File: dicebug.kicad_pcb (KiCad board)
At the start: 2 copper layers, 47.3 x 40.9 mm, 56 parts, among them J3 PMOD, Q1 SSM6N35AFE, U1 74LV163ADR, U2 MTCH1010, U3 74HCS7266DR, U4 MIC5205YM5, U5 iqs211a

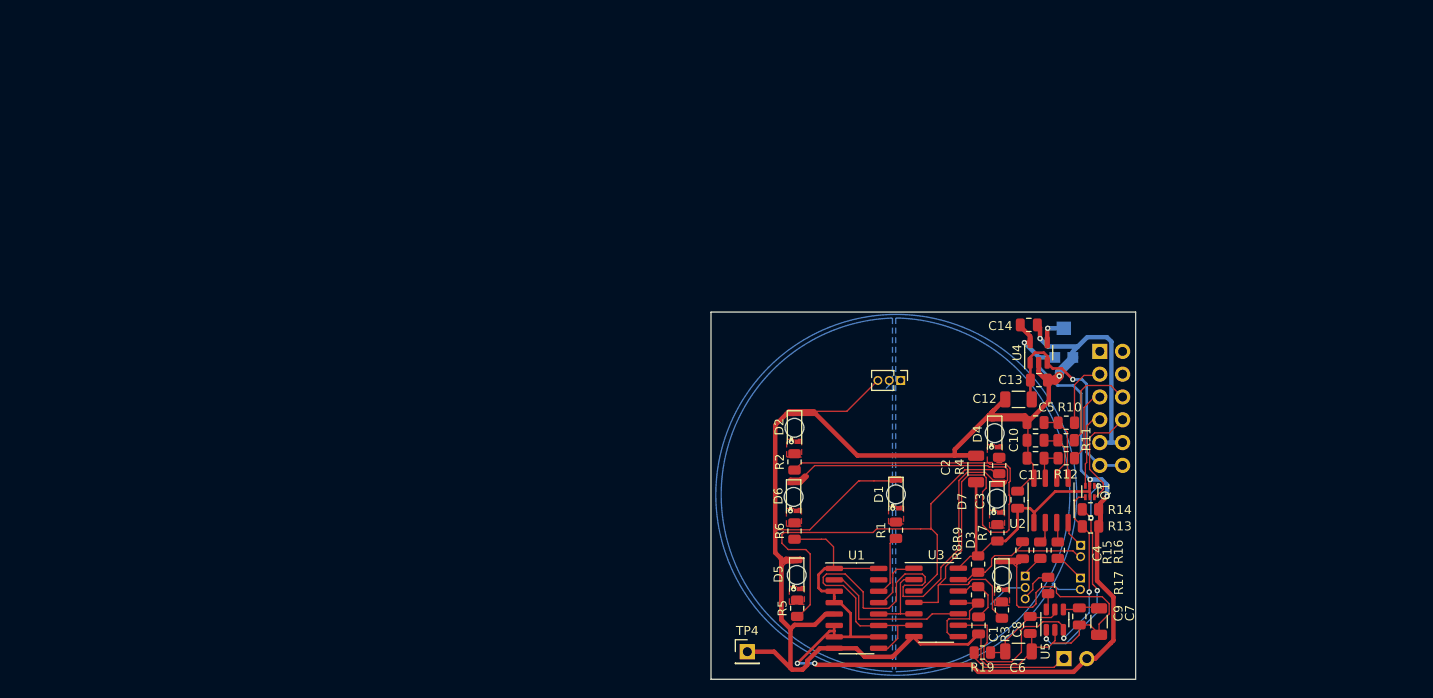
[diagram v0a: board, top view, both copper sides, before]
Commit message: almost finalized with individual LED resistors, though
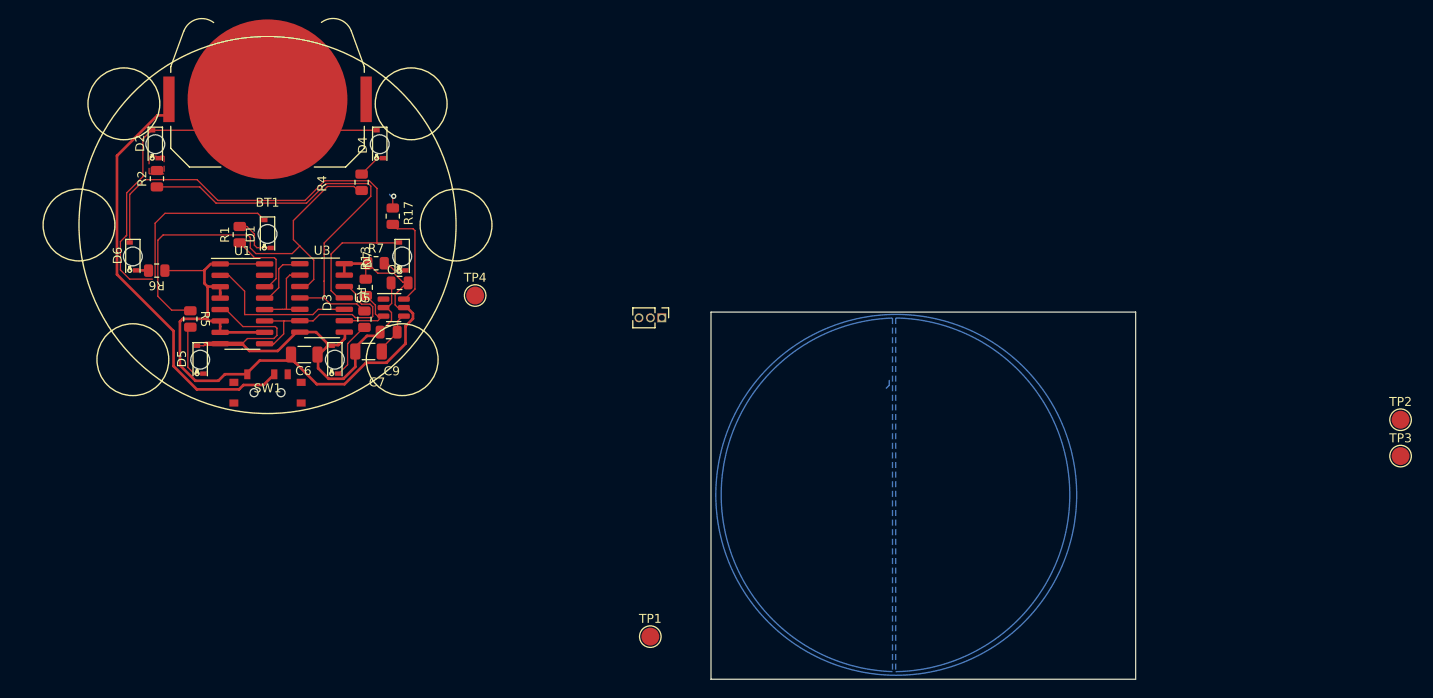
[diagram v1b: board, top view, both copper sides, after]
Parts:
- removed C1, C10, C11, C13, C5: 10n, Capacitor_SMD:C_0805_2012Metric
- removed C12, C2: 1u, Capacitor_SMD:C_1206_3216Metric
- removed C14: 1u, Capacitor_SMD:C_0805_2012Metric
- removed C3, C4: 100n, Capacitor_SMD:C_0805_2012Metric
- removed J3: PMOD, proj_footprints:PMOD_PinHeader_2x06_P2.54mm_Horizontal
- removed JP1: PWR_IQS, Connector_PinHeader_2.54mm:PinHeader_1x02_P2.54mm_Vertical
- removed JP2: MTCH, Connector_PinHeader_1.27mm:PinHeader_1x02_P1.27mm_Vertical
- removed JP3: i SENS m, Connector_PinHeader_1.27mm:PinHeader_1x03_P1.27mm_Vertical
- removed JP4: SHLD, Connector_PinHeader_1.27mm:PinHeader_1x02_P1.27mm_Vertical
- removed Q1: SSM6N35AFE, proj_footprints:SOT-563-adjusted
- removed R10, R11, R12, R14, R15, R8, R9: 100k, Resistor_SMD:R_0805_2012Metric
- removed R16: 1k, Resistor_SMD:R_0805_2012Metric
- removed R19: 40, Resistor_SMD:R_0805_2012Metric
- removed RV1: 100k, Potentiometer_SMD:Potentiometer_Bourns_TC33X_Vertical
- removed U2: MTCH1010, Package_SO:SOIC-8_3.9x4.9mm_P1.27mm
- removed U4: MIC5205YM5, Package_TO_SOT_SMD:SOT-23-5
- added BT1: CR2032, Battery:BatteryHolder_Keystone_3034_1x20mm, F.Cu at (100.0, 86.0)
- added SW1: SW_SPDT, proj_footprints:450404015514, F.Cu at (100.0, 118.7)
- added TP3: SCL, TestPoint:TestPoint_Pad_D2.0mm, F.Cu at (226.2, 125.7)
- added TP4: SDA, TestPoint:TestPoint_Pad_D2.0mm, F.Cu at (123.1, 107.9)
- TP1: renamed from TP4; value TestPoint -> GND; footprint Connector_PinHeader_2.54mm:PinHeader_1x01_P2.54mm_Vertical -> TestPoint:TestPoint_Pad_D2.0mm
- TP2: value Shield -> VCC; footprint sensors:tp_end -> TestPoint:TestPoint_Pad_D2.0mm; moved to F.Cu
- moved C7 86.8 mm to (111.3, 114.1), turned to 180 degrees
- moved C6 86.2 mm to (104.1, 114.4)
- moved R13 85.0 mm to (110.9, 106.9), turned to -90 degrees
- moved R17 83.8 mm to (114.0, 99.0)
- moved C9 83.2 mm to (113.5, 111.9), turned to 180 degrees
- moved U5 81.4 mm to (114.1, 109.2), turned to 0 degrees
- moved TP5 81.1 mm to (113.6, 96.6)
- moved R1 80.2 mm to (96.9, 101.1)
- moved C8 79.9 mm to (114.7, 106.5), turned to 180 degrees
- moved D6 78.3 mm to (85.0, 103.5)
- moved D3 78.1 mm to (107.5, 115.0)
- moved R3 78.0 mm to (110.8, 110.5), turned to -90 degrees
- moved D2 77.9 mm to (87.5, 91.0)
- moved R4 77.7 mm to (110.5, 95.2)
- moved R2 77.7 mm to (87.7, 94.8)
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- renumbered TP1 to TP5, TP3 to TP6
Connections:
- C6 pad 1: Net-(U5-VDD) -> +3V0
- C8 pad 1: Net-(U5-VDD) -> +3V0
- JP5 pad 1: Net-(JP3-C) -> /SENS_IQS
- TP2 pad 1: Net-(JP4-B) -> +3V0
- TP5 pad 1: Net-(JP3-C) -> /SENS_IQS
- U1 pad 11: Net-(D6-K) -> Net-(U1-Q3)
- U1 pad 9: Net-(D6-K) -> Net-(U1-Q3)
- U3 pad 11: Net-(R8-Pad2) -> Net-(D6-K)
- U3 pad 12: Net-(C1-Pad1) -> Net-(U1-Q3)
- U3 pad 13: Net-(JP2-B) -> +3V0
- U3 pad 6: Net-(D6-K) -> Net-(U1-Q3)
- U3 pad 8: Net-(R8-Pad2) -> GND
- U5 pad 5: Net-(U5-VDD) -> +3V0
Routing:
- net GND: track 299.4 -> 104.7 mm, vias 2 -> 0
- net +3V0: track 161.9 -> 94.3 mm, vias 5 -> 0
- net Net-(BT1-+): track 0.00 -> 46.8 mm
- net Net-(D6-K): track 95.9 -> 55.8 mm
- net Net-(U5-IO2/SDA): track 39.4 -> 8.01 mm, vias 2 -> 0
- net +3V3: track 25.5 -> 0.00 mm, vias 1 -> 0
- net Net-(U5-IO1/SCL): track 24.9 -> 0.00 mm, vias 4 -> 0
- net Net-(U1-Q3): track 0.00 -> 23.5 mm
- net Net-(R2-Pad1): track 71.3 -> 47.9 mm
- net Net-(JP2-B): track 16.9 -> 0.00 mm
- net Net-(J3-Pin_10): track 12.1 -> 0.00 mm
- net Net-(JP1-A): track 11.4 -> 0.00 mm
- net /CFG1: track 11.2 -> 0.00 mm
- net Net-(U5-VDD): track 10.2 -> 0.00 mm
- net Net-(R8-Pad2): track 9.69 -> 0.00 mm
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- added copper zone on B.Cu, net (none)
- added copper zone on B.Cu, net /SENS_IQS
- removed copper zone on F.Cu, net Net-(D1-A)
- removed copper zone on F.Cu, net Net-(D3-A)
- removed copper zone on F.Cu, net Net-(D4-A)
- removed copper zone on F.Cu, net Net-(D5-A)
- removed copper zone on F.Cu, net Net-(D6-A)
- removed copper zone on F.Cu, net Net-(D7-A)
- removed copper zone on B.Cu, net Net-(JP3-C)
- removed copper zone on B.Cu, net Net-(JP4-B)
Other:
- board text added: "dicebug-1.0"
- board text removed: "dicebug-dev-1.0"

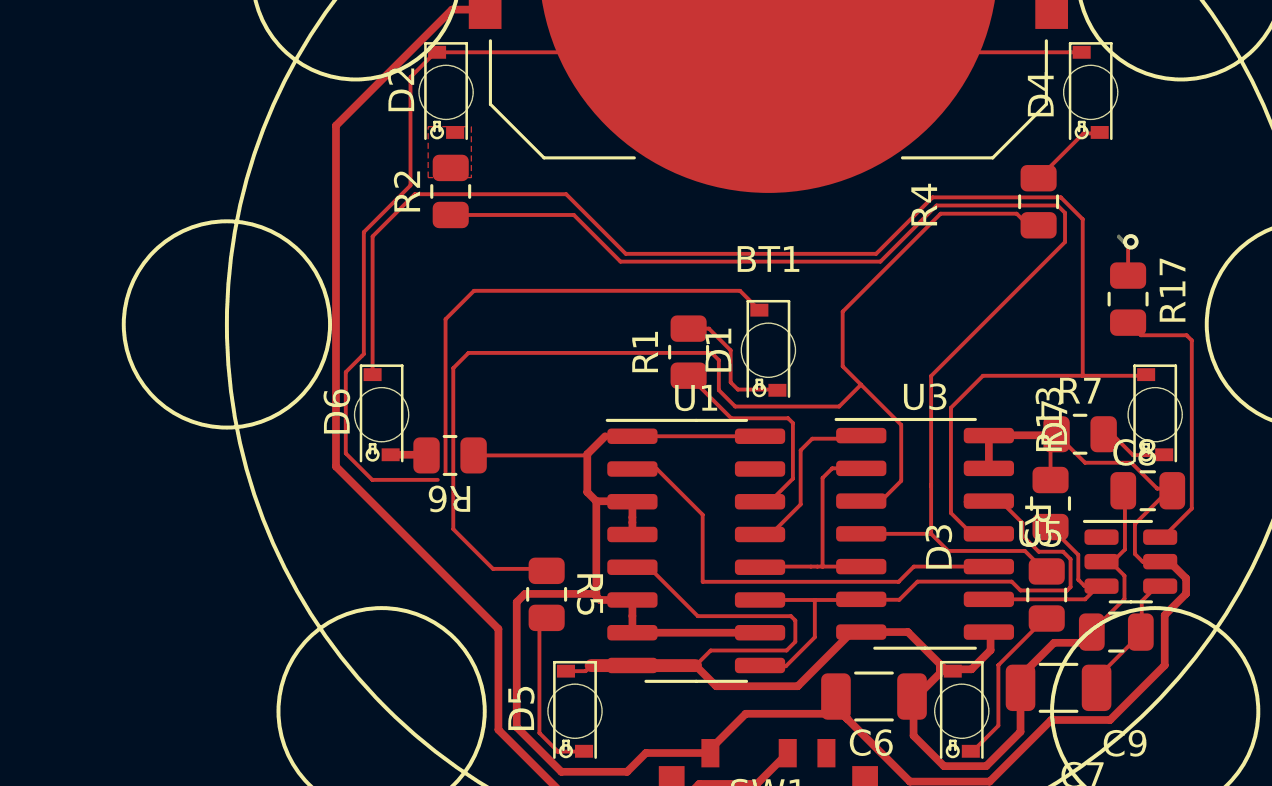
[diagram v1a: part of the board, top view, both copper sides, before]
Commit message: Drew schematics for R-array version; works fine.
No layout; the problem is that there is no reasonably priced
resistor array in SIOC-16 :-(
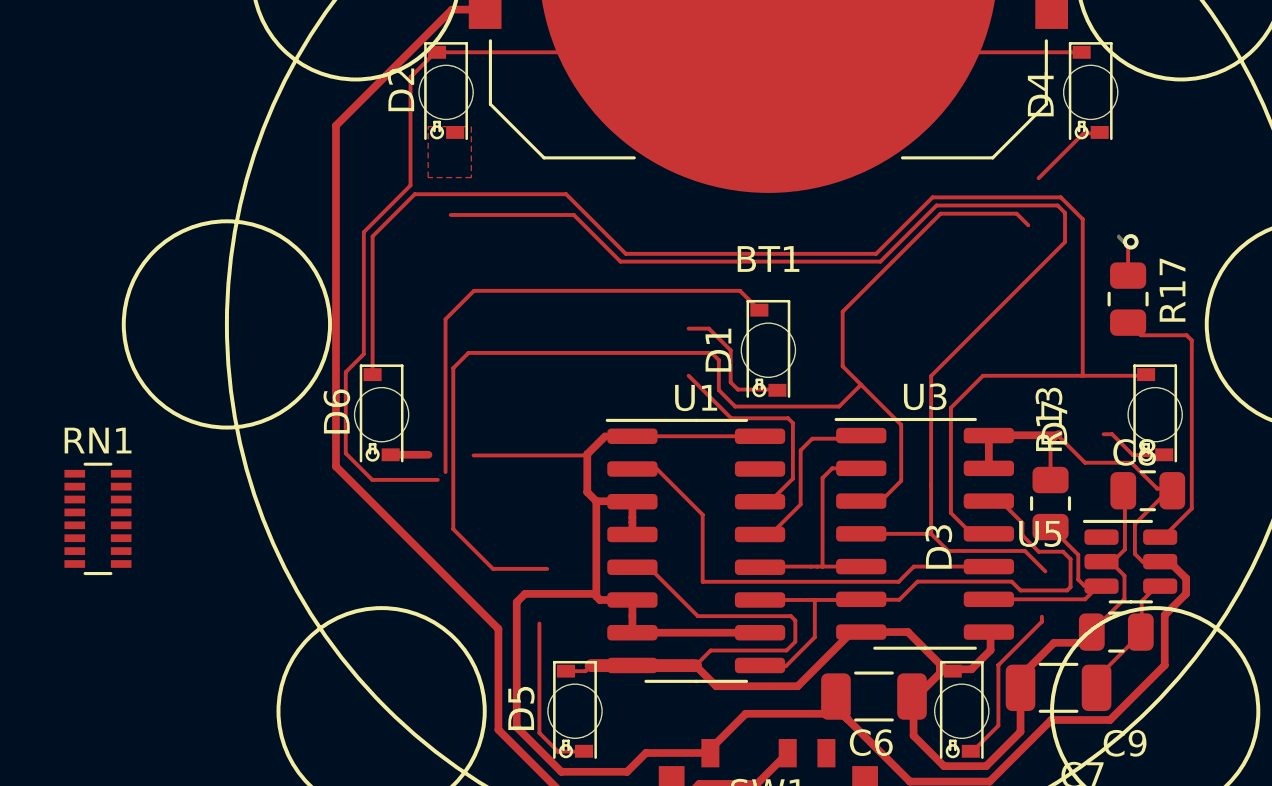
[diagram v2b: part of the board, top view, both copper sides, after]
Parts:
- removed R1, R2, R3, R4, R5, R6, R7: 2k8, Resistor_SMD:R_0805_2012Metric
- added RN1: 3k9, Resistor_SMD:R_Array_Convex_8x0602, F.Cu at (74.0, 107.5)
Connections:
- D6 pad 1: Net-(D6-K) -> GND
- D7 pad 1: Net-(D6-K) -> GND
- U3 pad 1: Net-(U1-Q1) -> Net-(U5-IO2/SDA)
- U3 pad 10: Net-(U1-CP) -> Net-(RN1-R2.1)
- U3 pad 11: Net-(D6-K) -> Net-(RN1-R1.1)
- U3 pad 12: Net-(U1-Q3) -> Net-(U1-Q2)
- U3 pad 13: +3V0 -> Net-(U1-Q1)
- U3 pad 2: Net-(U1-Q2) -> +3V0
- U3 pad 3: Net-(R4-Pad1) -> Net-(U1-CP)
- U3 pad 9: Net-(U5-IO2/SDA) -> Net-(U1-Q3)
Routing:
- net GND: track 104.7 -> 160.5 mm
- net Net-(D6-K): track 55.8 -> 0.00 mm
- net Net-(R4-Pad1): track 46.8 -> 0.00 mm
- net Net-(U1-CP): track 17.4 -> 64.2 mm
